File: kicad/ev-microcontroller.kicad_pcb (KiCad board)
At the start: 2 copper layers, 27.9 x 41.9 mm, 54 parts, among them IC1 MAX19777AZA+T, J1 MEM2051-00-195-00-A_REVC, J3 USB4105-GF-A, J6 Conn_02x12_Counter_Clockwise, U1 MAX77540AAWV+T, U2 DSC1001DI1-025.0000T, U3 TCKE812NA,RF, U4 RP2040, U6 TJA1441BTK/0Z, U7 MC6470, U8 WLCSP16_1P96X1P76X0P586_567SE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, U9 GD25Q40CEIGR

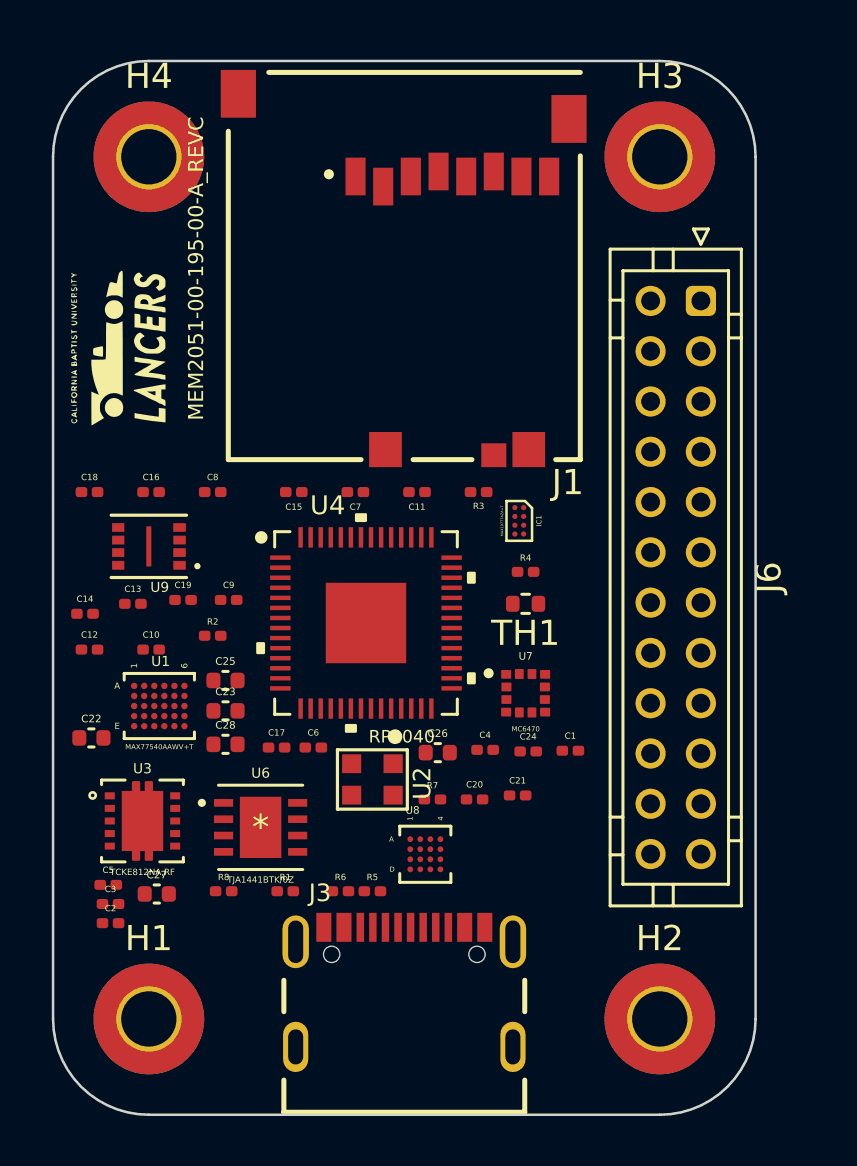
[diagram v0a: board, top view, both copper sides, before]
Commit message: Updated schematic with various changes
Increased size of small components
Updated title/spec sheet
Cleaned footprints
Other small changes as well
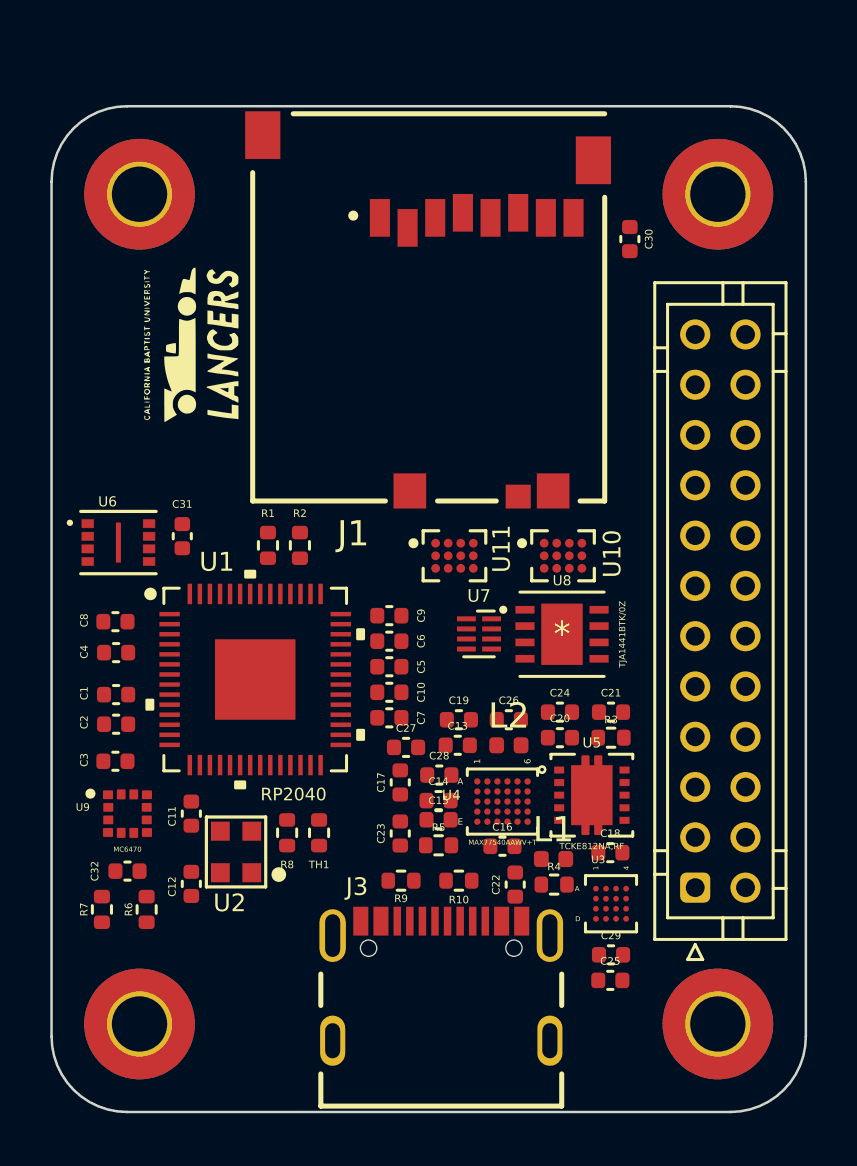
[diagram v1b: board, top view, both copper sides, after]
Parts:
- removed IC1: MAX19777AZA+T, personal:BGA8C35P4X2_143X86X37
- removed J6: Conn_02x12_Counter_Clockwise, Connector_JST:JST_PHD_B24B-PHDSS_2x12_P2.00mm_Vertical
- added C29: 22µF, personal:C_0402_1005Metric, F.Cu at (121.3, 111.8)
- added C30: 0.1µF, personal:C_0402_1005Metric, F.Cu at (122.0, 83.3)
- added C31: 0.1µF, personal:C_0402_1005Metric, F.Cu at (104.2, 95.1)
- added C32: 0.1µF, personal:C_0402_1005Metric, F.Cu at (102.0, 108.4)
- added J2: Conn_02x20_Odd_Even, Connector_JST:JST_PHD_B24B-PHDSS_2x12_P2.00mm_Vertical, F.Cu at (124.6, 109.1)
- added L1: 0.47µH, Inductor_SMD:L_0402_1005Metric, F.Cu at (119.0, 107.9)
- added L2: 0.47µH, Inductor_SMD:L_0402_1005Metric, F.Cu at (117.2, 103.4)
- added R10: 5.1k, personal:R_0402_1005Metric, F.Cu at (115.2, 108.8)
- added R9: 5.1k, personal:R_0402_1005Metric, F.Cu at (112.9, 108.8)
- added U10: MAX11613EWCT, personal:BGA12N50P3X4_188X221X69N, F.Cu at (119.3, 95.9)
- added U11: MAX11613EWCT, personal:BGA12N50P3X4_188X221X69N, F.Cu at (115.0, 95.9)
- added U5: TCKE812NA,RF, personal:WSON10B_TOS, F.Cu at (120.5, 105.4)
- C1, C10, C12, C13, C14, C2, C24, C4, C5, C6, C7, C8, C9: footprint personal:C_0201_0603Metric -> personal:C_0402_1005Metric
- C11: value 0.1µF -> 15pF; footprint personal:C_0201_0603Metric -> personal:C_0402_1005Metric
- C15, C16, C17: value 0.1µF -> 22µF; footprint personal:C_0201_0603Metric -> personal:C_0402_1005Metric
- C18: value 15pF -> 1µF; footprint personal:C_0201_0603Metric -> personal:C_0402_1005Metric
- C19: value 0.1µF -> 1µF; footprint personal:C_0201_0603Metric -> personal:C_0402_1005Metric
- C20: value 1µF -> 0.1µF; footprint personal:C_0201_0603Metric -> personal:C_0402_1005Metric
- C21: value 1µF -> 100pF; footprint personal:C_0201_0603Metric -> personal:C_0402_1005Metric
- C23, C25, C27: value 22µF -> 0.1µF
- C3: value 100pF -> 0.1µF; footprint personal:C_0201_0603Metric -> personal:C_0402_1005Metric
- R1: value 36k -> 27.4; footprint personal:R_0201_0603Metric -> personal:R_0402_1005Metric
- R2: footprint personal:R_0201_0603Metric -> personal:R_0402_1005Metric
- R3: value 27.4 -> 36k; footprint personal:R_0201_0603Metric -> personal:R_0402_1005Metric
- R4: value 470k -> 75k; footprint personal:R_0201_0603Metric -> personal:R_0402_1005Metric
- R5: value 5.1k -> 100k; footprint personal:R_0201_0603Metric -> personal:R_0402_1005Metric
- R6: value 5.1k -> 4.7k; footprint personal:R_0201_0603Metric -> personal:R_0402_1005Metric
- R7: value 75k -> 4.7k; footprint personal:R_0201_0603Metric -> personal:R_0402_1005Metric
- R8: value 100k -> 470k; footprint personal:R_0201_0603Metric -> personal:R_0402_1005Metric
- U1: value MAX77540AAWV+T -> RP2040; footprint personal:21-100414_W302P2Z+1_MXM -> personal:IC57_RP2040
- U3: value TCKE812NA,RF -> FPF3042UCX; footprint personal:WSON10B_TOS -> personal:FPF3042UCX
- U4: value RP2040 -> MAX77540AAWV+T; footprint personal:IC57_RP2040 -> personal:21-100414_W302P2Z+1_MXM
- U6: value TJA1441BTK/0Z -> GD25Q40CEIGR; footprint personal:HVSON8_TJA1441BTK_0Z_NXP -> personal:PSON50P200X300X50-9N
- U7: value MC6470 -> UM3202; footprint personal:PQFN50P200X200X100-12N -> personal:DFN-8_1.7x1.35mm_P0.4mm
- U8: value WLCSP16_1P96X1P76X0P586_567SE_ONS -> TJA1441BTK/0Z; footprint personal:FPF3042UCX -> personal:HVSON8_TJA1441BTK_0Z_NXP
- U9: value GD25Q40CEIGR -> MC6470; footprint personal:PSON50P200X300X50-9N -> personal:PQFN50P200X200X100-12N
- moved C18 25.2 mm to (121.2, 107.7)
- moved C16 19.8 mm to (116.9, 107.4)
- moved C25 19.4 mm to (121.2, 112.8)
- moved U3 18.9 mm to (121.3, 109.7)
- moved C1 18.2 mm to (101.6, 101.4)
- moved C22 17.8 mm to (117.4, 109.0), turned to 90 degrees
- moved C14 15.9 mm to (114.4, 105.6)
- moved C11 15.6 mm to (104.6, 106.1), turned to 90 degrees
- moved C4 15.2 mm to (101.6, 99.7)
- moved C15 14.2 mm to (114.4, 106.4), turned to 0 degrees
- moved C5 14.1 mm to (112.4, 100.3)
- moved C13 14.1 mm to (115.2, 103.4)
- moved R7 13.9 mm to (101.0, 109.9), turned to 90 degrees
- moved R1 13.8 mm to (107.6, 95.5), turned to 90 degrees
- moved U6 12.7 mm to (101.7, 95.4)
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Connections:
- C1 pad 1: V_SEL -> +3V3
- C10 pad 1: IO_FILTERING -> +1V1
- C11 pad 1: IO_FILTERING -> /MCU/CLOCK
- C12 pad 1: IO_FILTERING -> +3V3
- C13 pad 1: IO_FILTERING -> V_SEL
- C14 pad 1: +1V1 -> GND
- C14 pad 2: GND -> V_BUS
- C15 pad 1: +1V1 -> GND
- C15 pad 2: GND -> +5V
- C16 pad 1: +1V1 -> GND
- C16 pad 2: GND -> +5V
- C17 pad 1: IO_FILTERING -> GND
- C17 pad 2: GND -> +5V
- C18 pad 1: /MCU/CLOCK -> Net-(C18-Pad1)
- C19 pad 1: IO_FILTERING -> /Power/V_OUT
- C2 pad 1: GND -> +3V3
- C2 pad 2: V_BUS -> GND
- C20 pad 1: Net-(U1-PadE1) -> Net-(C20-Pad1)
- C20 pad 2: GND -> Net-(C20-Pad2)
- C21 pad 1: /Power/V_OUT -> Net-(C21-Pad1)
- C22 pad 2: +5V -> +3V3
- C23 pad 1: GND -> Net-(C23-Pad1)
- C23 pad 2: IO_FILTERING -> GND
- C24 pad 1: Net-(U1-PadD4) -> V_SEL
- C25 pad 1: GND -> Net-(C25-Pad1)
- C25 pad 2: +5V -> Net-(C25-Pad2)
- C26 pad 2: IO_FILTERING -> +3V3
- C27 pad 1: GND -> /Power/V_OUT
- C27 pad 2: +5V -> GND
- C28 pad 2: IO_FILTERING -> /Power/V_OUT
- C3 pad 1: Net-(C3-Pad1) -> +3V3
- C4 pad 1: V_SEL -> +3V3
- C5 pad 1: /Power/V_OUT -> +3V3
- C6 pad 1: IO_FILTERING -> +3V3
- C7 pad 1: IO_FILTERING -> +3V3
- C8 pad 1: IO_FILTERING -> +1V1
- C9 pad 1: IO_FILTERING -> +1V1
- J1 pad 4: IO_FILTERING -> +3V3
- J1 pad 9: unconnected-(J1-Pad9) -> GPIO_CD
- R1 pad 1: Net-(U3-Pad10) -> Net-(R1-Pad1)
- R1 pad 2: GND -> DP
- R2 pad 2: DP -> DN
- R3 pad 2: DN -> GND
- R4 pad 1: IO_FILTERING -> Net-(R4-Pad1)
- R4 pad 2: GPIO_TEMP -> GND
- R5 pad 1: Net-(J3-PadA5) -> GND
- R5 pad 2: GND -> Net-(R5-Pad2)
- R6 pad 1: GND -> +3V3
- R6 pad 2: Net-(J3-PadB5) -> SDA_1
- R7 pad 1: Net-(U1-PadD2) -> +3V3
- R7 pad 2: GND -> SCL_1
- R8 pad 1: GND -> +3V3
- R8 pad 2: Net-(U1-PadD1) -> GPIO_TEMP
- U2 pad 4: IO_FILTERING -> +3V3
- U6 pad 1: unconnected-(U6-Pad1) -> QSPI_SS
- U6 pad 2: unconnected-(U6-Pad2) -> QSPI_SD1
- U6 pad 3: unconnected-(U6-Pad3) -> QSPI_SD2
- U6 pad 4: unconnected-(U6-Pad4) -> GND
- U6 pad 5: unconnected-(U6-Pad5) -> QSPI_SD0
- U6 pad 6: unconnected-(U6-Pad6) -> QSPI_SCLK
- U6 pad 7: unconnected-(U6-Pad7) -> QSPI_SD3
- U6 pad 8: unconnected-(U6-Pad8) -> +3V3
- U6 pad 9: unconnected-(U6-Pad9) -> (no net)
- U7 pad 1: unconnected-(U7-Pad1) -> (no net)
- U7 pad 2: unconnected-(U7-Pad2) -> (no net)
- U7 pad 3: unconnected-(U7-Pad3) -> (no net)
- U7 pad 4: unconnected-(U7-Pad4) -> (no net)
- U7 pad 5: unconnected-(U7-Pad5) -> (no net)
- U7 pad 6: unconnected-(U7-Pad6) -> (no net)
- U7 pad 7: unconnected-(U7-Pad7) -> (no net)
- U7 pad 8: unconnected-(U7-Pad8) -> (no net)
- U9 pad 1: unconnected-(U9-Pad1) -> GND
- U9 pad 2: QSPI_SD1 -> SDA_1
- U9 pad 3: QSPI_SD2 -> Net-(C32-Pad2)
- U9 pad 4: GND -> unconnected-(U9-Pad4)
- U9 pad 5: QSPI_SD0 -> unconnected-(U9-Pad5)
- U9 pad 6: QSPI_SCLK -> unconnected-(U9-Pad6)
- U9 pad 7: QSPI_SD3 -> Net-(C32-Pad2)
- U9 pad 8: IO_FILTERING -> unconnected-(U9-Pad8)
- U9 pad 9: (no net) -> GND
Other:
- board size 27.9 x 41.9 mm -> 30 x 40 mm

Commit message: Modified size of pcb board
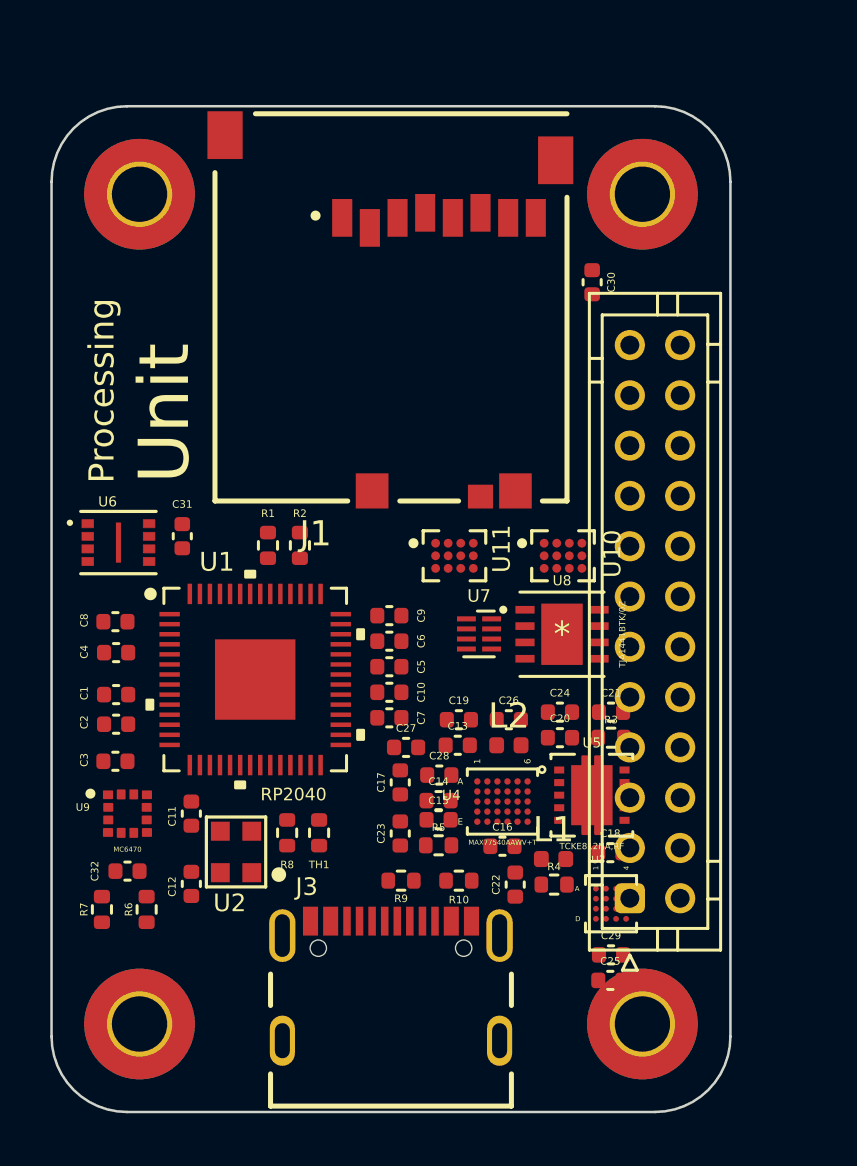
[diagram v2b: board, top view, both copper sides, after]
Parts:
- removed G***: LOGO, graphics:cbu-small
- moved H2 3.00 mm to (122.5, 114.5)
- moved H3 3.00 mm to (122.5, 81.5)
- moved J2 2.63 mm to (122.0, 109.5)
- moved C30 2.28 mm to (120.5, 85.0)
- moved J3 2.00 mm to (112.5, 115.2)
- moved J1 1.50 mm to (112.5, 86.1)
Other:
- board size 30 x 40 mm -> 27 x 40 mm
- board text added: "Processing"
- board text added: "Unit"
